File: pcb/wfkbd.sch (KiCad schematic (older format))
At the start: 0 parts

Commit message: Add base pro data
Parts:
- added D1, D10, D11, D12, D13, D14, D15, D16, D17, D18, D19, D2, D20, D21, D22, D23, D24, D25, D26, D27, D28, D29, D3, D30, D4, D5, D6, D7, D8, D9: D, symbol D
- added J1: MJ-4PP-9, symbol MJ-4PP-9
- added P1: LED, symbol Conn_01x03
- added R1, R2: R, symbol R
- added RSW1: RESET, symbol SW_PUSH
- added SW1, SW10, SW11, SW12, SW13, SW14, SW15, SW16, SW17, SW18, SW19, SW2, SW20, SW21, SW22, SW23, SW24, SW25, SW26, SW27, SW28, SW29, SW3, SW30, SW4, SW5, SW6, SW7, SW8, SW9: KEY, symbol SW_PUSH
- added U1: ProMicro, symbol ProMicro
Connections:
- new net: D1.2 (A), SW1.2
- new net: D2.2 (A), SW2.2
- new net: D3.2 (A), SW3.2
- new net: D4.2 (A), SW4.2
- new net: D5.2 (A), SW5.2
- new net: D6.2 (A), SW6.2
- new net: D7.2 (A), SW7.2
- new net: D8.2 (A), SW8.2
- new net: D9.2 (A), SW9.2
- new net: D10.2 (A), SW10.2
- new net: D11.2 (A), SW11.2
- new net: D12.2 (A), SW12.2
- new net: D13.2 (A), SW13.2
- new net: D14.2 (A), SW14.2
- new net: D15.2 (A), SW15.2
- new net: D16.2 (A), SW16.2
- new net: D17.2 (A), SW17.2
- new net: D18.2 (A), SW18.2
- new net: D19.2 (A), SW19.2
- new net: D20.2 (A), SW20.2
- new net: D21.2 (A), SW21.2
- new net: D22.2 (A), SW22.2
- new net: D23.2 (A), SW23.2
- new net: D24.2 (A), SW24.2
- new net: D25.2 (A), SW25.2
- new net: D26.2 (A), SW26.2
- new net: D27.2 (A), SW27.2
- new net: D28.2 (A), SW28.2
- new net: D29.2 (A), SW29.2
- new net: D30.2 (A), SW30.2
- new net GND: J1.C, P1.1 (Pin_1), RSW1.2, U1.23 (GND), U1.3 (GND), U1.4 (GND)
- new net VCC: J1.D, P1.3 (Pin_3), R1.1, R2.1, U1.21 (VCC)
- new net col0: SW1.1, SW13.1, SW19.1, SW25.1, SW7.1, U1.20 (F4)
- new net col1: SW14.1, SW2.1, SW20.1, SW26.1, SW8.1, U1.19 (F5)
- new net col2: SW15.1, SW21.1, SW27.1, SW3.1, SW9.1, U1.18 (F6)
- new net col3: SW10.1, SW16.1, SW22.1, SW28.1, SW4.1, U1.17 (F7)
- new net col4: SW11.1, SW17.1, SW23.1, SW29.1, SW5.1, U1.16 (B1)
- new net col5: SW12.1, SW18.1, SW24.1, SW30.1, SW6.1, U1.15 (B3)
- new net data: J1.B, U1.2 (RX)
- new net led: P1.2 (Pin_2), U1.1 (TX)
- new net reset: RSW1.1, U1.22 (RST)
- new net row0: D1.1 (K), D2.1 (K), D3.1 (K), D4.1 (K), D5.1 (K), D6.1 (K), U1.7 (D4)
- new net row1: D10.1 (K), D11.1 (K), D12.1 (K), D7.1 (K), D8.1 (K), D9.1 (K), U1.8 (C6)
- new net row2: D13.1 (K), D14.1 (K), D15.1 (K), D16.1 (K), D17.1 (K), D18.1 (K), U1.9 (D7)
- new net row3: D19.1 (K), D20.1 (K), D21.1 (K), D22.1 (K), D23.1 (K), D24.1 (K), U1.10 (E6)
- new net row4: D25.1 (K), D26.1 (K), D27.1 (K), D28.1 (K), D29.1 (K), D30.1 (K), U1.11 (B4)
- new net scl: R2.2, U1.6 (SCL)
- new net sda: R1.2, U1.5 (SDA)
- no-connect marks 0 -> 5

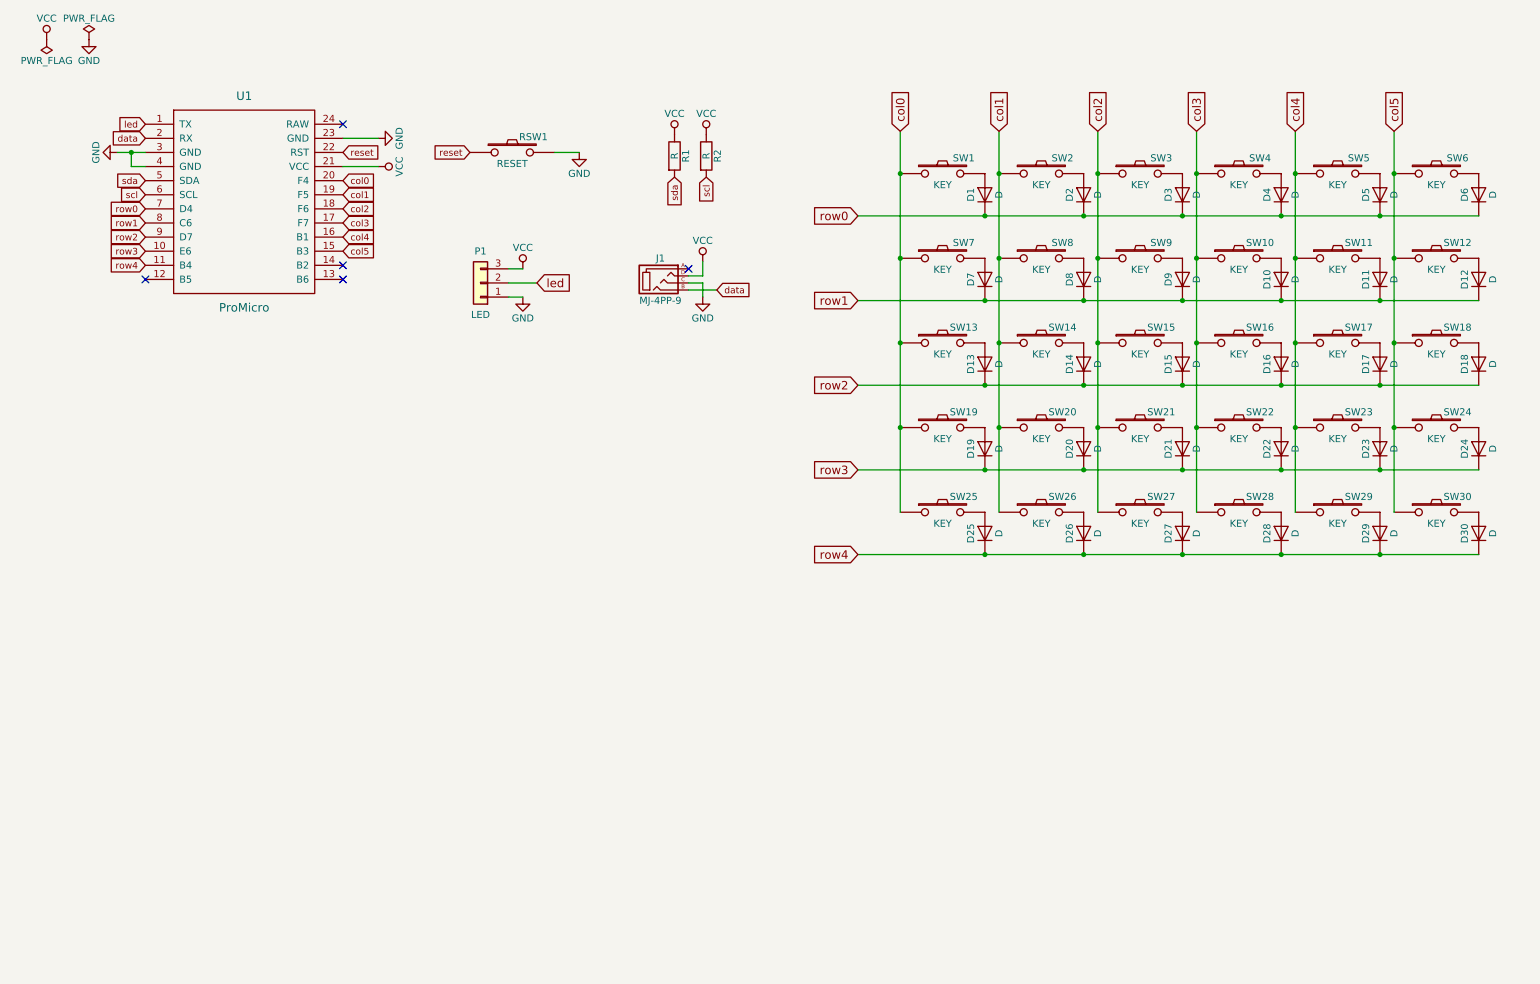
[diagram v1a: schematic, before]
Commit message: Scalable cols/rows
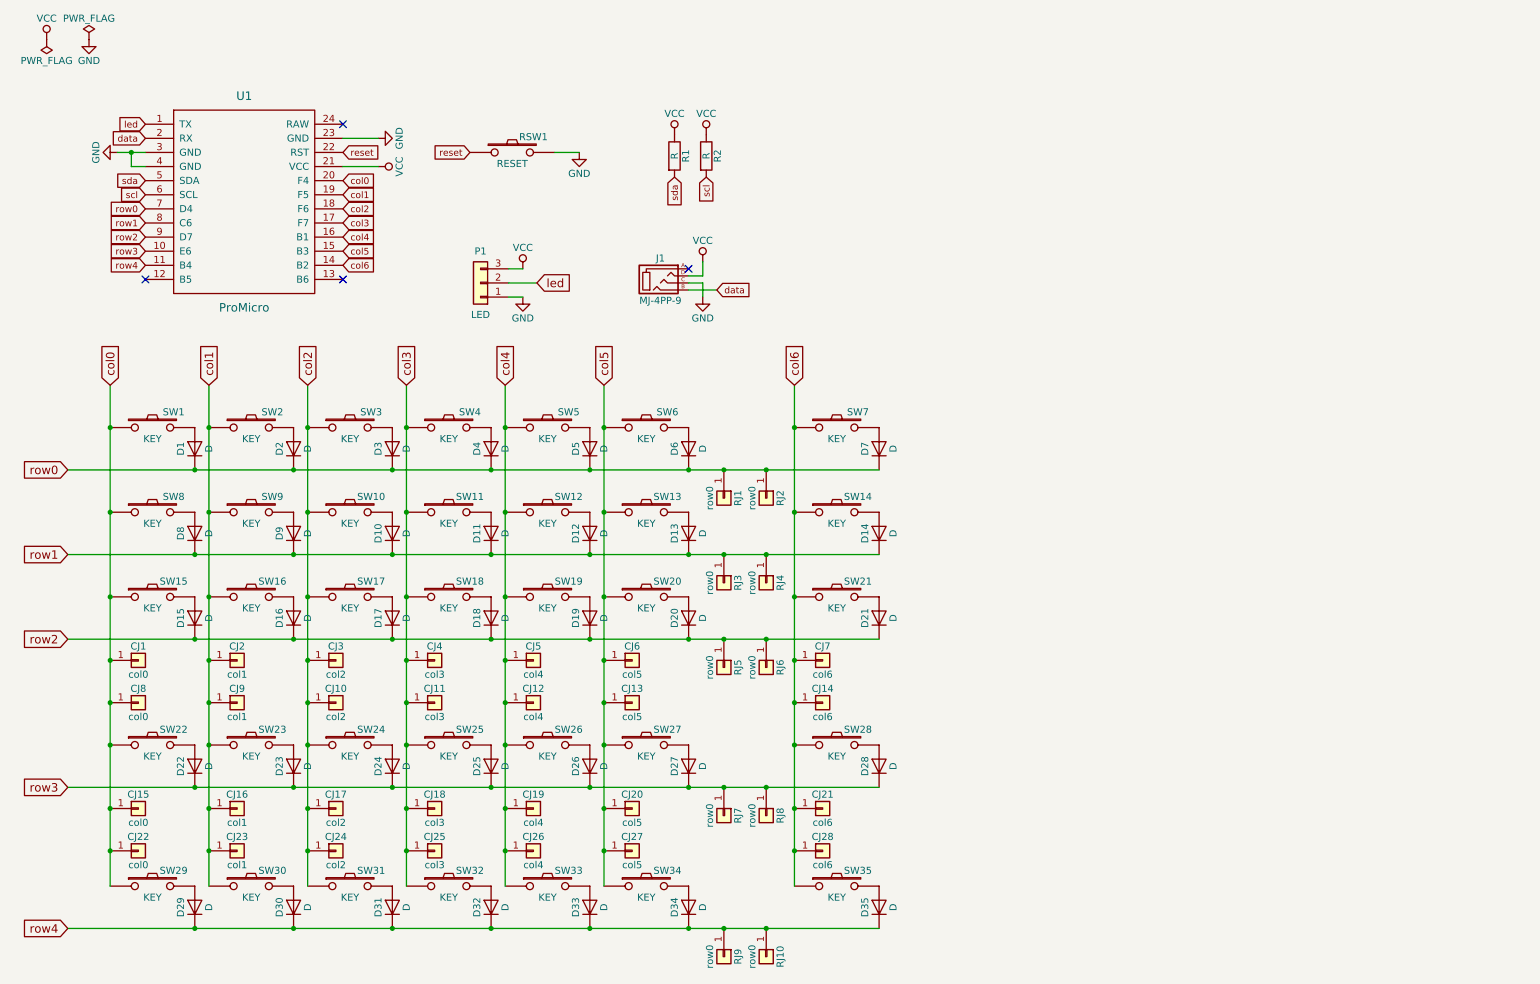
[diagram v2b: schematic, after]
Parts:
- added CJ1, CJ15, CJ22, CJ8: col0, symbol Conn_01x01
- added CJ10, CJ17, CJ24, CJ3: col2, symbol Conn_01x01
- added CJ11, CJ18, CJ25, CJ4: col3, symbol Conn_01x01
- added CJ12, CJ19, CJ26, CJ5: col4, symbol Conn_01x01
- added CJ13, CJ20, CJ27, CJ6: col5, symbol Conn_01x01
- added CJ14, CJ21, CJ28, CJ7: col6, symbol Conn_01x01
- added CJ16, CJ2, CJ23, CJ9: col1, symbol Conn_01x01
- added D14, D21, D28, D35, D7: D, symbol D
- added RJ1, RJ10, RJ2, RJ3, RJ4, RJ5, RJ6, RJ7, RJ8, RJ9: row0, symbol Conn_01x01
- added SW14, SW21, SW28, SW35, SW7: KEY, symbol SW_PUSH
- renumbered D9 to D10, D10 to D11, D11 to D12, D12 to D13, D13 to D15, D14 to D16, D15 to D17, D16 to D18, D17 to D19, D18 to D20, D19 to D22, D20 to D23, D21 to D24, D22 to D25, D23 to D26, D24 to D27, D25 to D29, D26 to D30, D27 to D31, D28 to D32, D29 to D33, D30 to D34, D7 to D8, D8 to D9, SW9 to SW10, SW10 to SW11, SW11 to SW12, SW12 to SW13, SW13 to SW15, SW14 to SW16, SW15 to SW17, SW16 to SW18, SW17 to SW19, SW18 to SW20, SW19 to SW22, SW20 to SW23, SW21 to SW24, SW22 to SW25, SW23 to SW26, SW24 to SW27, SW25 to SW29, SW26 to SW30, SW27 to SW31, SW28 to SW32, SW29 to SW33, SW30 to SW34, SW7 to SW8, SW8 to SW9
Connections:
- net col0: now also CJ1.1 (Pin_1), CJ15.1 (Pin_1), CJ22.1 (Pin_1), CJ8.1 (Pin_1)
- net col1: now also CJ16.1 (Pin_1), CJ2.1 (Pin_1), CJ23.1 (Pin_1), CJ9.1 (Pin_1)
- net col2: now also CJ10.1 (Pin_1), CJ17.1 (Pin_1), CJ24.1 (Pin_1), CJ3.1 (Pin_1)
- net col3: now also CJ11.1 (Pin_1), CJ18.1 (Pin_1), CJ25.1 (Pin_1), CJ4.1 (Pin_1)
- net col4: now also CJ12.1 (Pin_1), CJ19.1 (Pin_1), CJ26.1 (Pin_1), CJ5.1 (Pin_1)
- net col5: now also CJ13.1 (Pin_1), CJ20.1 (Pin_1), CJ27.1 (Pin_1), CJ6.1 (Pin_1)
- net row0: now also D7.1 (K), RJ1.1 (Pin_1), RJ2.1 (Pin_1)
- net row1: now also D14.1 (K), RJ3.1 (Pin_1), RJ4.1 (Pin_1)
- net row2: now also D21.1 (K), RJ5.1 (Pin_1), RJ6.1 (Pin_1)
- net row3: now also D28.1 (K), RJ7.1 (Pin_1), RJ8.1 (Pin_1)
- net row4: now also D35.1 (K), RJ10.1 (Pin_1), RJ9.1 (Pin_1)
- net col6: now reaches U1.14 (B2)
- net col6: now also CJ14.1 (Pin_1), CJ21.1 (Pin_1), CJ28.1 (Pin_1), CJ7.1 (Pin_1), SW14.1, SW21.1, SW28.1, SW35.1, SW7.1
- new net: D7.2 (A), SW7.2
- new net: D14.2 (A), SW14.2
- new net: D21.2 (A), SW21.2
- new net: D28.2 (A), SW28.2
- new net: D35.2 (A), SW35.2
- no-connect marks 5 -> 4
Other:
- moved on the sheet: D1, D10, D11, D12, D13, D15, D16, D17, D18, D19, D2, D20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

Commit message: Add nets
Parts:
- CJ1, CJ10, CJ11, CJ12, CJ13, CJ14, CJ15, CJ16, CJ17, CJ18, CJ19, CJ2, CJ20, CJ21, CJ22, CJ23, CJ24, CJ25, CJ26, CJ27, CJ28, CJ3, CJ4, CJ5, CJ6, CJ7, CJ8, CJ9, RJ1, RJ10, RJ2, RJ3, RJ4, RJ5, RJ6, RJ7, RJ8, RJ9: footprint (none) -> kbd:1pin_conn
- D1, D10, D11, D12, D13, D14, D15, D16, D17, D18, D19, D2, D20, D21, D22, D23, D24, D25, D26, D27, D28, D29, D3, D30, D31, D32, D33, D34, D35, D4, D5, D6, D7, D8, D9: footprint (none) -> kbd:D3_TH_SMD
- J1: footprint (none) -> kbd:MJ-4PP-9
- P1: footprint (none) -> kbd:StripLED_rev
- R1, R2: footprint (none) -> kbd:R
- RSW1: footprint (none) -> kbd:SW_3.5x6.0_TH
- SW1, SW10, SW11, SW12, SW13, SW14, SW15, SW16, SW17, SW18, SW19, SW2, SW20, SW21, SW22, SW23, SW24, SW25, SW26, SW27, SW28, SW29, SW3, SW30, SW31, SW32, SW33, SW34, SW35, SW4, SW5, SW6, SW7, SW8, SW9: footprint (none) -> kbd:MX_ALPS_PG1350_noLed
- U1: footprint (none) -> kbd:ProMicro

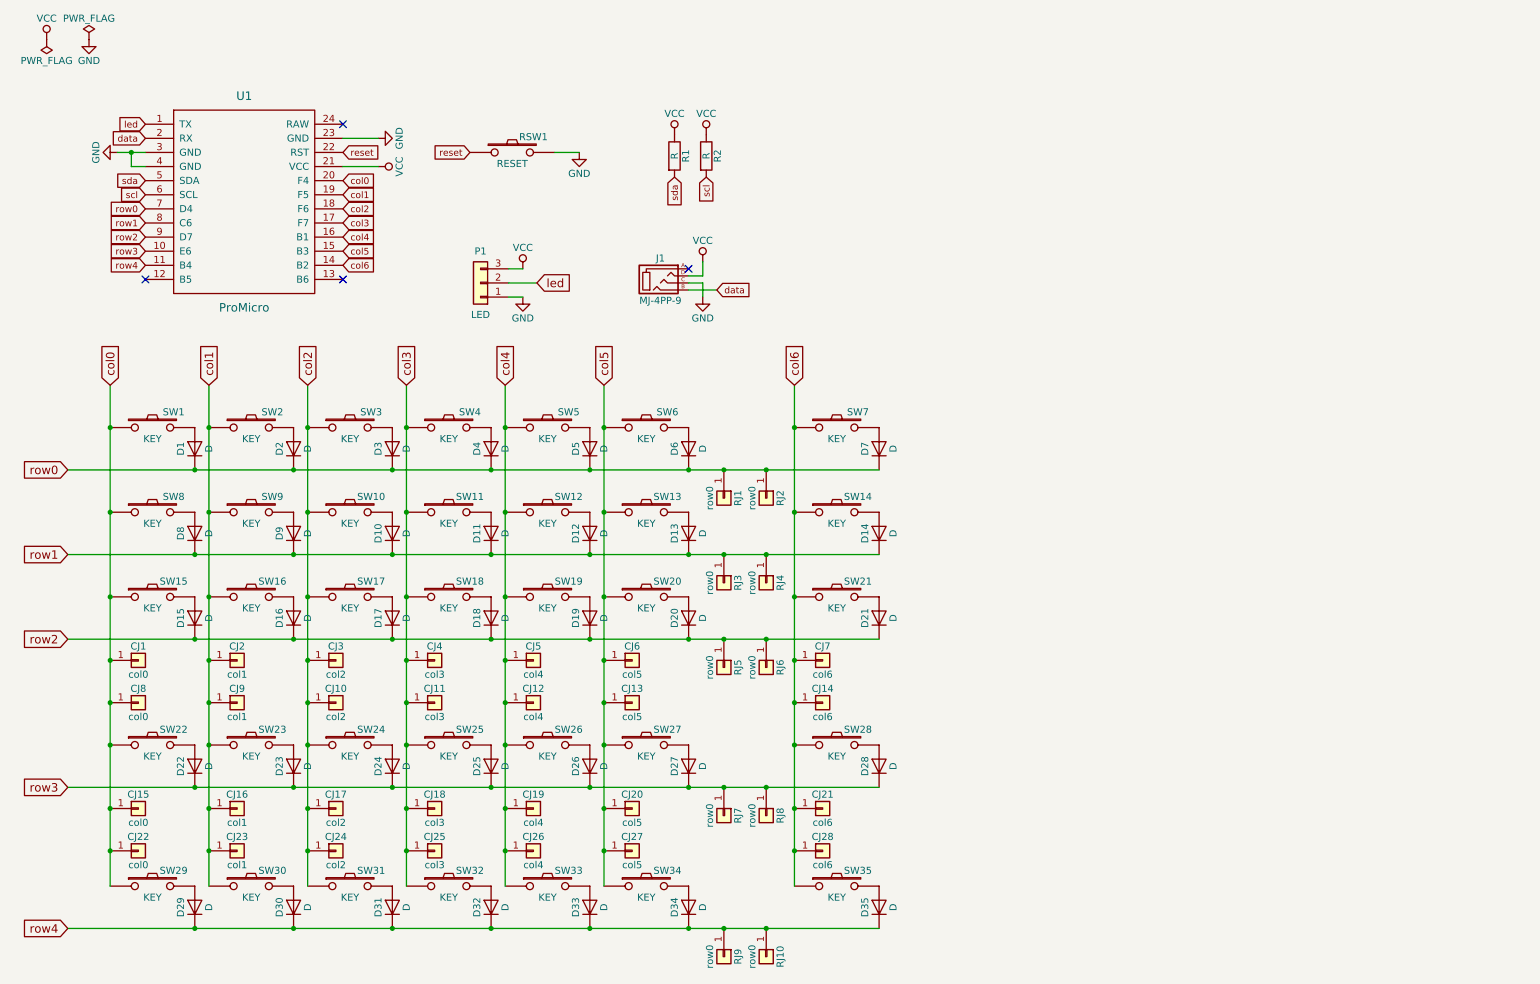
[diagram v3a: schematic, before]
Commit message: Add splid line
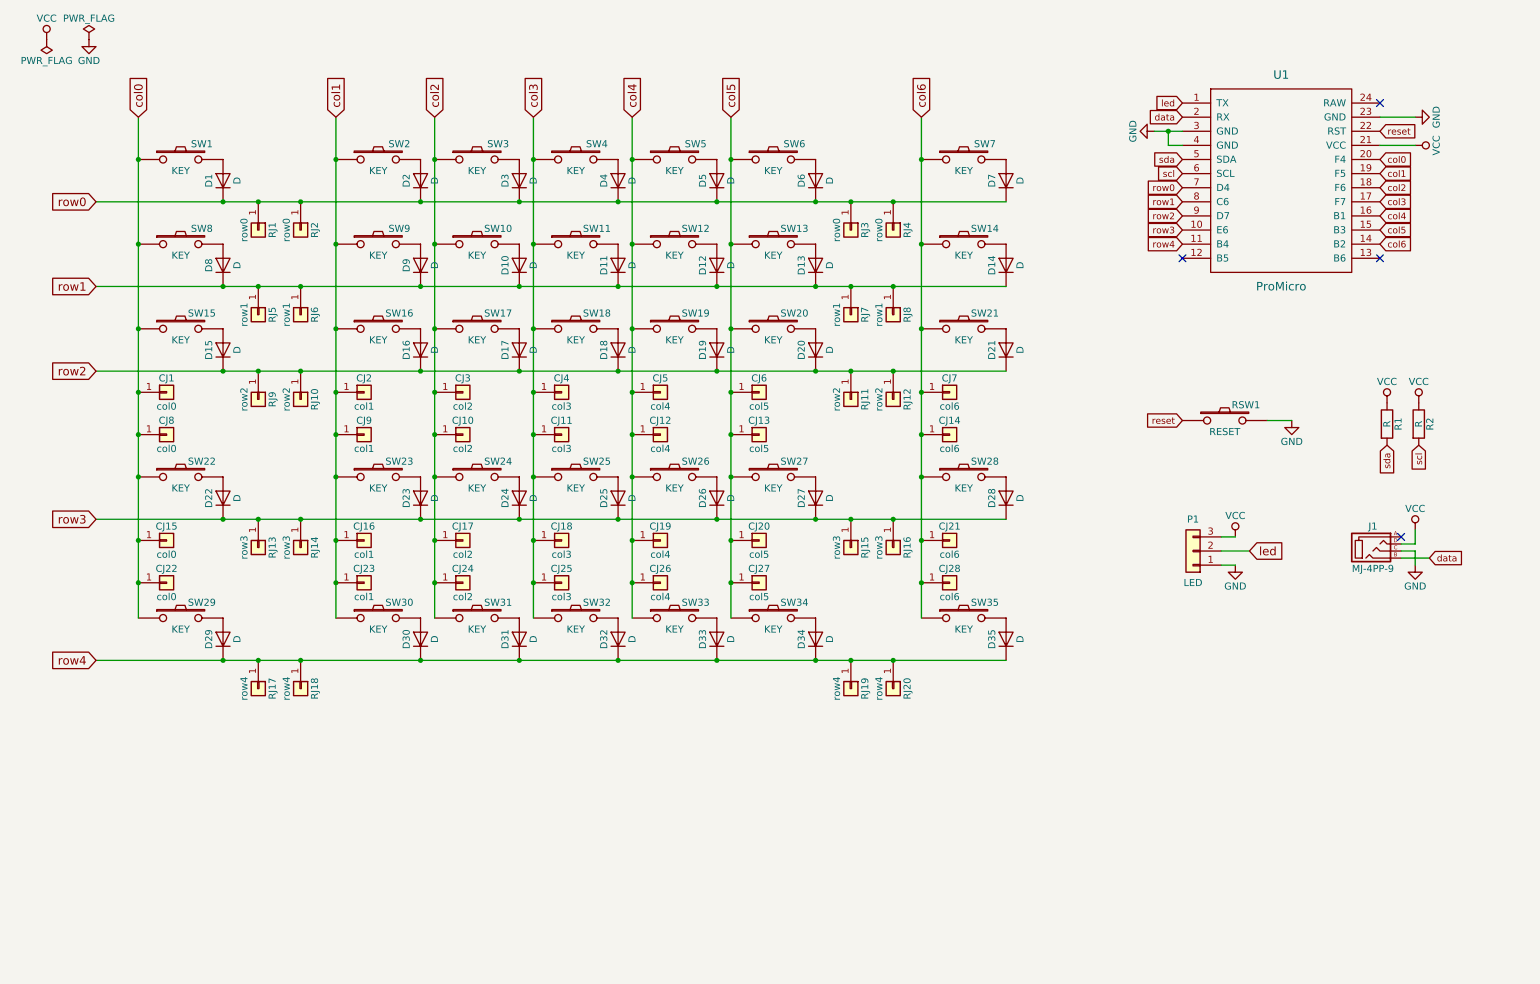
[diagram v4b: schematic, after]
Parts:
- added RJ1, RJ2: row0, kbd:1pin_conn, symbol Conn_01x01
- added RJ10, RJ9: row2, kbd:1pin_conn, symbol Conn_01x01
- added RJ13, RJ14: row3, kbd:1pin_conn, symbol Conn_01x01
- added RJ17, RJ18: row4, kbd:1pin_conn, symbol Conn_01x01
- added RJ5, RJ6: row1, kbd:1pin_conn, symbol Conn_01x01
- RJ11: renamed from RJ5; value row0 -> row2
- RJ12: renamed from RJ6; value row0 -> row2
- RJ15: renamed from RJ7; value row0 -> row3
- RJ16: renamed from RJ8; value row0 -> row3
- RJ19: renamed from RJ9; value row0 -> row4
- RJ20: renamed from RJ10; value row0 -> row4
- RJ7: renamed from RJ3; value row0 -> row1
- RJ8: renamed from RJ4; value row0 -> row1
- renumbered RJ1 to RJ3, RJ2 to RJ4
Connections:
- net row0: now also RJ1.1 (Pin_1), RJ2.1 (Pin_1)
- net row1: now also RJ5.1 (Pin_1), RJ6.1 (Pin_1)
- net row2: now also RJ10.1 (Pin_1), RJ9.1 (Pin_1)
- net row3: now also RJ13.1 (Pin_1), RJ14.1 (Pin_1)
- net row4: now also RJ17.1 (Pin_1), RJ18.1 (Pin_1)
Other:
- moved on the sheet: CJ1, CJ10, CJ11, CJ12, CJ13, CJ14, CJ15, CJ16, CJ17, CJ18, CJ19, CJ2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

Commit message: Add pcbnew files
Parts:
- removed CJ1, CJ15, CJ22, CJ8: col0, kbd:1pin_conn, symbol Conn_01x01
- removed CJ10, CJ17, CJ24, CJ3: col2, kbd:1pin_conn, symbol Conn_01x01
- removed CJ11, CJ18, CJ25, CJ4: col3, kbd:1pin_conn, symbol Conn_01x01
- removed CJ12, CJ19, CJ26, CJ5: col4, kbd:1pin_conn, symbol Conn_01x01
- removed CJ13, CJ20, CJ27, CJ6: col5, kbd:1pin_conn, symbol Conn_01x01
- removed CJ14, CJ21, CJ28, CJ7: col6, kbd:1pin_conn, symbol Conn_01x01
- removed CJ16, CJ2, CJ23, CJ9: col1, kbd:1pin_conn, symbol Conn_01x01
- removed P1: LED, kbd:StripLED_rev, symbol Conn_01x03
- removed RJ1, RJ2, RJ3, RJ4: row0, kbd:1pin_conn, symbol Conn_01x01
- removed RJ10, RJ11, RJ12, RJ9: row2, kbd:1pin_conn, symbol Conn_01x01
- removed RJ13, RJ14, RJ15, RJ16: row3, kbd:1pin_conn, symbol Conn_01x01
- removed RJ17, RJ18, RJ19, RJ20: row4, kbd:1pin_conn, symbol Conn_01x01
- removed RJ5, RJ6, RJ7, RJ8: row1, kbd:1pin_conn, symbol Conn_01x01
- added C1: VCC, kbd:1pin_conn, symbol Conn_01x01
- added C2: GND, kbd:1pin_conn, symbol Conn_01x01
- added C3: LED, kbd:1pin_conn, symbol Conn_01x01
- added J?: Conn_01x01, symbol Conn_01x01
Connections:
- net GND: now also C2.1 (Pin_1)
- net VCC: now also C1.1 (Pin_1)
- net led: now also C3.1 (Pin_1)
- net row4: now also J?.1 (Pin_1)
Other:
- moved on the sheet: D1, D11, D12, D13, D14, D15, D16, D18, D19, D2, D20, D21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
